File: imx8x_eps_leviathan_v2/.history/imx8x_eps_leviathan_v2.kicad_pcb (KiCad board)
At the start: 6 copper layers, 100 x 100 mm, 430 parts, among them CN1 DF11-16DP-2DSA(08), CN2 DF11-16DP-2DSA(08), J1 Conn_01x01_Socket, J10 BTH-070-02-L-D-A, J2 Conn_01x01_Socket, J3 Conn_01x01_Socket, J4 Conn_01x01_Socket, J5 DF11-16DP-2DSA, J9 BTH-070-02-L-D-A, Q1 IRLML6401, Q2 BSS138, SW1 SW_DIP_x01, SW2 KMR221GLFS, T1 WE-RJ45_7499111121A, T2 WE-RJ45_7499111121A, U1 XT60PW-F_C428722, U10 LT8612EUDE#PBF, U11 TCA4307DGKR, U12 INA260AIPWR, U13 TPS1HB08BQPWPRQ1, U14 LT8612EUDE#PBF, U15 INA260AIPWR, U16 TLV1704, U17 TLV1704, U18 BD2204GUL-E2, U19 CAT93C66VI-GT3, U2 MCP9808T-E/MS, U20 FT2232HL, U21 LP38693MP-ADJ/NOPB, U22 TXS0101DCKR, U23 TXS0101DCKR, U24 TXS0108EPWR, U25 DP83867CRRGZR, U26 MCP1824T-ADJE/OT, U27 TLV71310PDQNR, U28 74LVC2G07GW, U29 TPS22917DBVR, U3 MCP9808T-E/MS, U30 TLV62569PDDCR, U31 TXS0108EPWR, U32 TCA4307DGKR, U4 MCP9808T-E/MS, U5 TPS1HB08BQPWPRQ1, U6 LT8612EUDE#PBF, U7 INA260AIPWR, U8 TPS1HB08BQPWPRQ1, U9 LTC6902, Y1 12MHz, Y3 25MHz

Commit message: updates
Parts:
- C87: value 10nF -> 2.2nF
- moved R85 2.50 mm to (155.3, 124.0)
- moved SW1 2.50 mm to (159.2, 125.7)
- moved USB1 2.50 mm to (159.0, 131.5)
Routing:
- net Net-(U20-ADBUS1): track 0.00 -> 4.08 mm
- net Net-(U20-ACBUS5): track 0.00 -> 3.83 mm
- net Net-(U20-ACBUS4): track 0.00 -> 3.82 mm
- net Net-(U20-ADBUS2): track 0.00 -> 3.65 mm
- net Net-(U20-ACBUS3): track 0.00 -> 3.05 mm
- net Net-(U20-ADBUS3): track 0.00 -> 2.92 mm
- net Net-(U20-ACBUS6): track 0.00 -> 2.63 mm
- net Net-(U20-BDBUS0): track 0.00 -> 2.61 mm
- net Net-(U20-ADBUS4): track 0.00 -> 2.60 mm
- net Net-(U20-BDBUS3): track 0.00 -> 2.60 mm
- net Net-(U20-ACBUS2): track 0.00 -> 2.46 mm
- net Net-(U20-ACBUS7): track 0.00 -> 2.31 mm
- net Net-(U20-BDBUS1): track 0.00 -> 2.29 mm
- net Net-(U20-BDBUS2): track 0.00 -> 2.28 mm
- net Net-(U20-ADBUS5): track 0.00 -> 2.02 mm
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
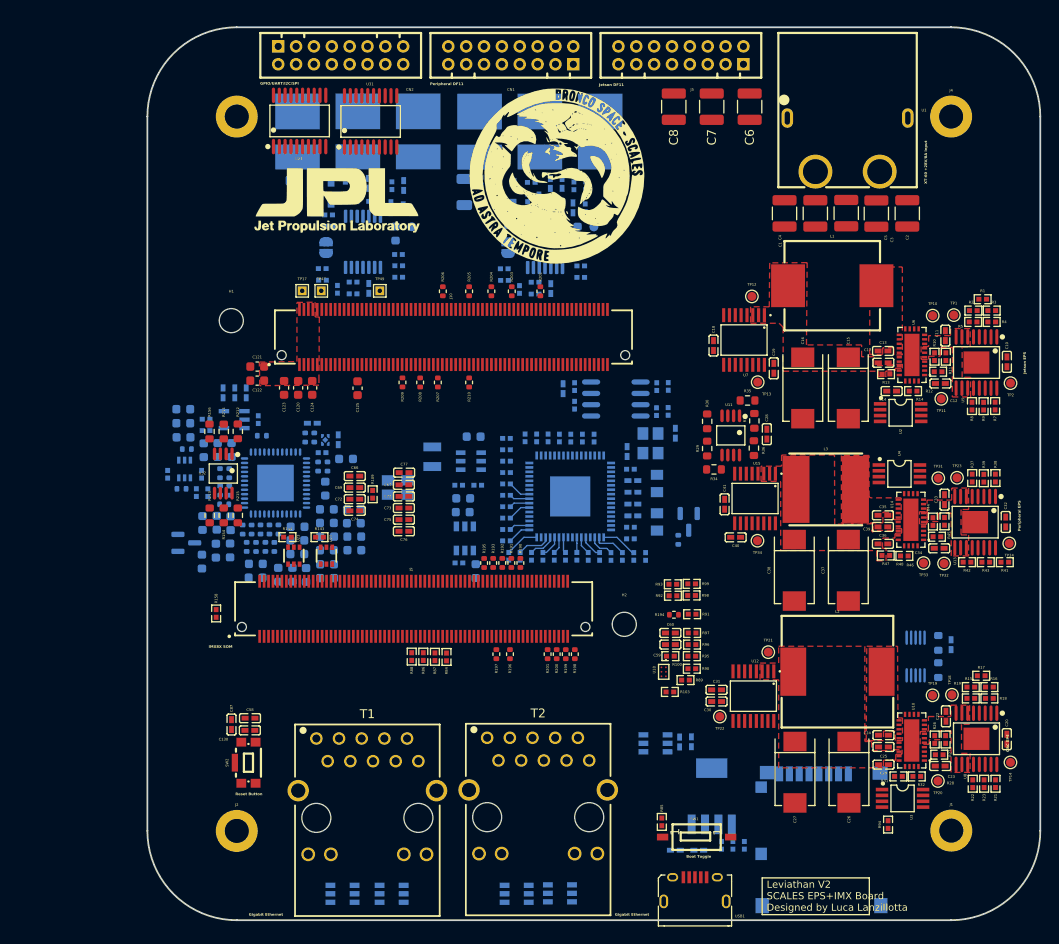
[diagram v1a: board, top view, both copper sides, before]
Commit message: Goodies
Updated USB to USB C. Added Diodes for USB. Improved Layout. Ready for some routing.
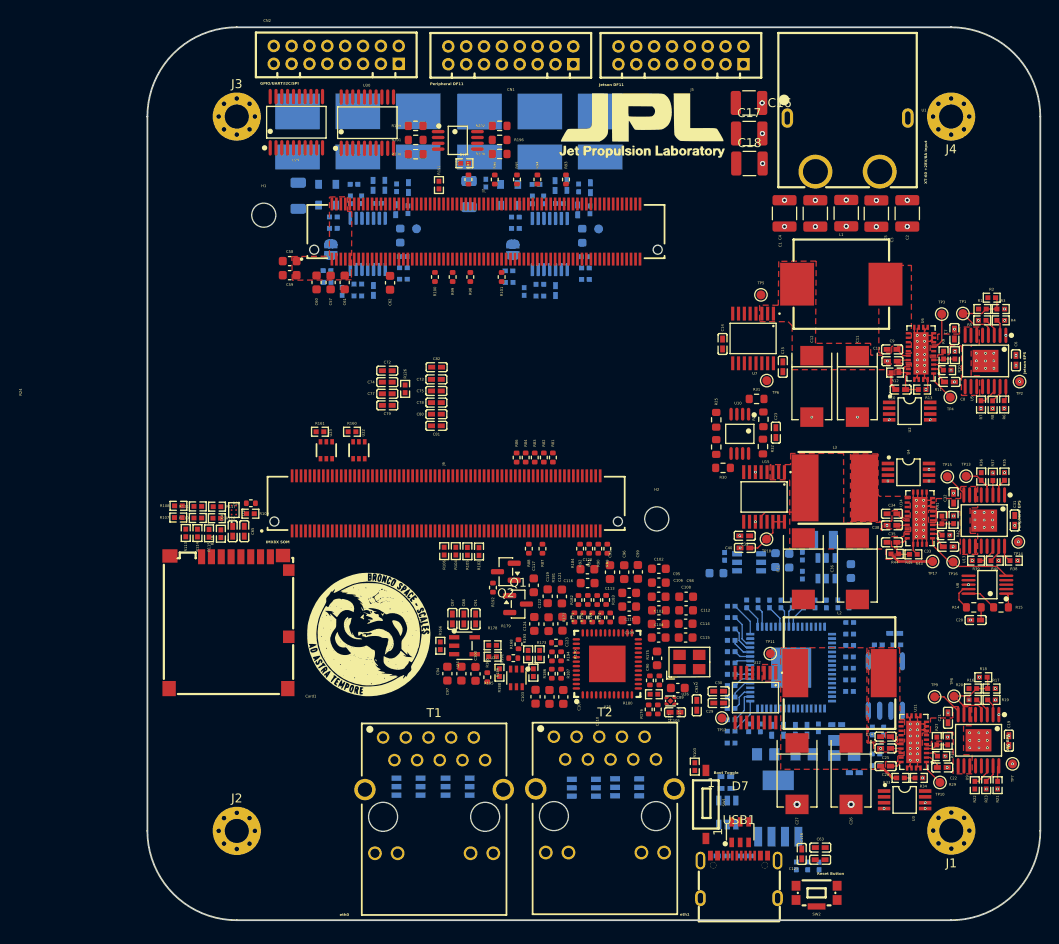
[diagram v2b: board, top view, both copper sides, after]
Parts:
- removed the C68 at (151.4, 82.5)
- removed the C7 at (160.8, 43.9)
- removed the C8 at (156.6, 43.9)
- removed the R103 at (156.2, 109.4)
- removed the TP17 at (115.0, 64.5)
- removed TP47, TP49: TestPoint, TestPoint:TestPoint_THTPad_1.0x1.0mm_Drill0.5mm
- added C17: 10u, Capacitor_SMD:C_1210_3225Metric, F.Cu at (165.0, 46.9)
- added C18: 10u, Capacitor_SMD:C_1210_3225Metric, F.Cu at (165.1, 50.2)
- added C70: 12pF, EPS:C0402, B.Cu at (174.9, 113.1)
- added D7: USBLC6-2SC6, imx8_carrier_board_footprints:SOT-23-6_L2.9-W1.6-P0.95-LS2.8-BL, F.Cu at (164.0, 125.1)
- C100: renamed from C97; moved to F.Cu
- C101: renamed from C98; moved to F.Cu
- C102: renamed from C99; moved to F.Cu
- C103: renamed from C100; moved to F.Cu
- C104: renamed from C101; moved to F.Cu
- C105: renamed from C85; moved to F.Cu
- C106: renamed from C102; moved to F.Cu
- C107: renamed from C103; moved to F.Cu
- C108: renamed from C104; moved to F.Cu
- C109: renamed from C105; moved to F.Cu
- C110: renamed from C106; moved to F.Cu
- C111: renamed from C107; moved to F.Cu
- C112: renamed from C108; moved to F.Cu
- C113: renamed from C109; moved to F.Cu
- C114: renamed from C110; moved to F.Cu
- C115: renamed from C111; moved to F.Cu
- C116: renamed from C112; moved to F.Cu
- C117: renamed from C113; moved to F.Cu
- C119: renamed from C114; moved to F.Cu
- C120: renamed from C115; moved to F.Cu
- C121: renamed from C116; moved to F.Cu
- C122: renamed from C117; moved to F.Cu
- C123: renamed from C118; moved to F.Cu
- C124: renamed from C119; moved to F.Cu
- C20: renamed from C21; moved to F.Cu
- C87: renamed from C82; moved to F.Cu
- C88: renamed from C83; moved to F.Cu
- C89: renamed from C88; moved to F.Cu
- C90: renamed from C89; moved to F.Cu
- C91: renamed from C86; moved to F.Cu
- C92: renamed from C90; moved to F.Cu
- C93: renamed from C84; moved to F.Cu
- C94: renamed from C91; moved to F.Cu
- C95: renamed from C92; moved to F.Cu
- C96: renamed from C93; moved to F.Cu
- C97: renamed from C94; moved to F.Cu
- C98: renamed from C95; moved to F.Cu
- C99: renamed from C96; moved to F.Cu
- Card1, R169, R170, R171, R172, R173, R174, R175, R176, R177, U25: moved to F.Cu
- J1, J2, J3, J4: footprint MountingHole:MountingHole_2.7mm_M2.5_DIN965_Pad -> MountingHole:MountingHole_2.7mm_M2.5_Pad_Via
- Q1, Q2: footprint imx8_carrier_board_footprints:SOT-23 -> Package_TO_SOT_SMD:SOT-23; moved to F.Cu
- R14: renamed from R24; moved to F.Cu
- R15: renamed from R25; moved to F.Cu
- R165: renamed from R167; moved to F.Cu
- R166: renamed from R148; moved to F.Cu
- R167: renamed from R168; moved to F.Cu
- R168: renamed from R189; moved to F.Cu
- R178: renamed from R155; moved to F.Cu
- R179: renamed from R157; moved to F.Cu
- R180: renamed from R151; moved to F.Cu
- R181: renamed from R179; moved to F.Cu
- R182: renamed from R180; moved to F.Cu
- R183: renamed from R181; moved to F.Cu
- R184: renamed from R182; moved to F.Cu
- R186: renamed from R183; moved to F.Cu
- R187: renamed from R184; moved to F.Cu
- R188: renamed from R149; moved to F.Cu
- R189: renamed from R150; moved to F.Cu
- R190: renamed from R152; moved to F.Cu
- R191: renamed from R153; moved to F.Cu
- R192: renamed from R185; moved to F.Cu
- R193: renamed from R186; moved to F.Cu
- R194: renamed from R187; moved to F.Cu
- R195: renamed from R188; moved to F.Cu
- U24: renamed from U26; moved to F.Cu
- U26: renamed from U27; moved to F.Cu
- U27: renamed from U28; moved to F.Cu
- U8: renamed from U9; moved to F.Cu
- USB1: value 10118194-0001LF -> TYPE-C 16PIN 2MD; footprint imx8_carrier_board_footprints:MICRO-USB-SMD_10118194-0001LF -> imx8_carrier_board_footprints:USB-C-SMD_TYPE-C-6PIN-2MD-073
- Y2: renamed from Y3; moved to F.Cu
- moved R112 88.0 mm to (133.2, 50.2), turned to 0 degrees
- moved Card1 70.6 mm to (106.8, 101.6), turned to 180 degrees
- moved SW2 65.7 mm to (172.6, 132.3), turned to 180 degrees
- moved C118 65.5 mm to (170.9, 127.5)
- moved C125 65.5 mm to (173.0, 128.2)
- moved C63 65.5 mm to (173.0, 126.8)
- moved R108 60.3 mm to (101.1, 88.6), turned to 180 degrees
- moved R107 59.6 mm to (101.1, 89.9), turned to 180 degrees
- moved R113 58.3 mm to (101.9, 91.6), turned to 90 degrees
- moved R114 56.8 mm to (103.3, 91.6), turned to 90 degrees
- moved G*** 55.5 mm to (122.5, 102.9)
- moved R115 55.2 mm to (104.6, 91.6), turned to 90 degrees
- moved R197 54.1 mm to (130.3, 52.6)
- moved R110 53.9 mm to (103.3, 89.9)
- moved R111 53.9 mm to (103.3, 88.6)
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- renumbered C14 to C10, C15 to C11, C87 to C118, C16 to C12, C130 to C125, C17 to C13, C126 to C130, C127 to C131, C128 to C132, C129 to C133, C18 to C14, C19 to C15, C6 to C16, C20 to C19, C22 to C21, C23 to C22, C28 to C23, C29 to C28, C30 to C29, C31 to C30, C32 to C31, C33 to C32, C34 to C33, C35 to C34, C36 to C35, C37 to C36, C38 to C37, C39 to C38, C40 to C39, C41 to C40, C42 to C41, C43 to C42, C44 to C43, C45 to C44, C46 to C45, C47 to C46, C48 to C47, C49 to C48, C50 to C49, C51 to C50, C52 to C51, C53 to C52, C54 to C53, C55 to C54, C56 to C55, C57 to C56, C120 to C57, C121 to C58, C122 to C59, C10 to C6, C123 to C60, C124 to C61, C125 to C62, C58 to C63, C59 to C64, C60 to C65, C61 to C66, C62 to C67, C63 to C68, C64 to C69, C11 to C7, C65 to C71, C66 to C72, C67 to C73, C69 to C74, C70 to C75, C71 to C76, C72 to C77, C73 to C78, C74 to C79, C12 to C8, C75 to C80, C76 to C81, C77 to C82, C78 to C83, C79 to C84, C80 to C85, C81 to C86, C13 to C9, D4 to D1, D5 to D2, D6 to D3, D7 to D4, D8 to D5, D9 to D6, J9 to J6, J10 to J7, R2 to R1, R11 to R10, R209 to R100, R210 to R101, R84 to R102, R85 to R103, R86 to R104, R87 to R105, R88 to R106, R89 to R107, R90 to R108, R91 to R109, R12 to R11, R92 to R110, R93 to R111, R94 to R112, R95 to R113, R96 to R114, R97 to R115, R98 to R116, R99 to R117, R100 to R118, R13 to R12, R102 to R120, R104 to R121, R105 to R122, R106 to R123, R107 to R124, R108 to R125, R109 to R126, R110 to R127, R111 to R128, R112 to R129, R14 to R13, R113 to R130, R114 to R131, R115 to R132, R116 to R133, R117 to R134, R118 to R135, R119 to R136, R120 to R137, R121 to R138, R122 to R139, R123 to R140, R124 to R141, R125 to R142, R126 to R143, R127 to R144, R128 to R145, R129 to R146, R130 to R147, R131 to R148, R132 to R149, R133 to R150, R134 to R151, R135 to R152, R136 to R153, R137 to R154, R138 to R155, R139 to R156, R140 to R157, R141 to R158, R142 to R159, R15 to R16, R143 to R160, R144 to R161, R145 to R162, R146 to R163, R147 to R164, R16 to R17, R17 to R18, R18 to R19, R154 to R196, R158 to R197, R156 to R198, R212 to R199, R1 to R2, R19 to R20, R213 to R200, R214 to R201, R215 to R202, R6 to R212, R20 to R213, R29 to R24, R30 to R25, R33 to R26, R26 to R27, R27 to R28, R28 to R29, R34 to R30, R35 to R31, R36 to R32, R31 to R33, R32 to R34, R38 to R35, R37 to R36, R39 to R37, R41 to R38, R42 to R39, R43 to R40, R44 to R41, R45 to R42, R46 to R43, R47 to R44, R48 to R45, R49 to R46, R50 to R47, R51 to R48, R52 to R49, R53 to R50, R54 to R51, R55 to R52, R56 to R53, R57 to R54, R58 to R55, R59 to R56, R60 to R57, R61 to R58, R62 to R59, R7 to R6, R63 to R60, R64 to R61, R65 to R62, R66 to R63, R67 to R64, R68 to R65, R69 to R66, R70 to R67, R71 to R68, R72 to R69, R8 to R7, R73 to R70, R74 to R71, R75 to R72, R76 to R73, R77 to R74, R78 to R75, R79 to R76, R80 to R77, R81 to R78, R82 to R79, R9 to R8, R83 to R80, R190 to R81, R191 to R82, R192 to R83, R193 to R84, R194 to R85, R195 to R86, R196 to R87, R197 to R88, R198 to R89, R10 to R9, R199 to R90, R200 to R91, R201 to R92, R202 to R93, R203 to R94, R204 to R95, R205 to R96, R206 to R97, R207 to R98, R208 to R99, TP20 to TP10, TP21 to TP11, TP22 to TP12, TP23 to TP13, TP24 to TP14, TP31 to TP15, TP32 to TP16, TP33 to TP17, TP34 to TP18, TP36 to TP19, TP42 to TP20, TP10 to TP3, TP11 to TP4, TP12 to TP5, TP13 to TP6, TP14 to TP7, TP18 to TP8, TP19 to TP9, U11 to U10, U10 to U11, U32 to U28, U24 to U29, U31 to U30, U29 to U31, U30 to U32, U8 to U9
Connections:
- C71 pad 1: GND -> /IMX8XQXP SCALES Mariner Carrier Board/Debug USB - UART/FTDI_OSCO
- C71 pad 2: /IMX8XQXP SCALES Mariner Carrier Board/Debug USB - UART/FTDI_OSCO -> GND
- CN2 pad 1: Net-(U24-B1) -> GND
- CN2 pad 10: Net-(U31-B5) -> Net-(U30-B4)
- CN2 pad 11: Net-(U24-B6) -> Net-(U29-B3)
- CN2 pad 12: Net-(U31-B6) -> Net-(U30-B3)
- CN2 pad 13: Net-(U24-B7) -> Net-(U29-B2)
- CN2 pad 14: Net-(U31-B7) -> I2C3_USR_SCL
- CN2 pad 15: GND -> Net-(U29-B1)
- CN2 pad 16: GND -> I2C3_USR_SDA
- CN2 pad 2: I2C3_USR_SDA -> GND
- CN2 pad 3: Net-(U24-B2) -> Net-(U29-B7)
- CN2 pad 4: I2C3_USR_SCL -> Net-(U30-B7)
- CN2 pad 5: Net-(U24-B3) -> Net-(U29-B6)
- CN2 pad 6: Net-(U31-B3) -> Net-(U30-B6)
- CN2 pad 7: Net-(U24-B4) -> Net-(U29-B5)
- CN2 pad 8: Net-(U31-B4) -> Net-(U30-B5)
- CN2 pad 9: Net-(U24-B5) -> Net-(U29-B4)
- JP1 pad 1: Net-(JP1-A) -> unconnected-(JP1-A-Pad1)
- JP1 pad 2: ~{WD_EN_OBC} -> unconnected-(JP1-B-Pad2)
- JP2 pad 1: Net-(JP2-A) -> unconnected-(JP2-A-Pad1)
- JP2 pad 2: ~{WD_EN_JETSON} -> unconnected-(JP2-B-Pad2)
- U16 pad 13: Net-(JP1-A) -> unconnected-(U16-Pad13)
- U17 pad 13: Net-(JP2-A) -> unconnected-(U17-Pad13)
- U29 pad 13: Net-(U24-B7) -> Net-(U29-B7)
- U29 pad 14: Net-(U24-B6) -> Net-(U29-B6)
- U29 pad 15: Net-(U24-B5) -> Net-(U29-B5)
- U29 pad 16: Net-(U24-B4) -> Net-(U29-B4)
- U29 pad 17: Net-(U24-B3) -> Net-(U29-B3)
- U29 pad 18: Net-(U24-B2) -> Net-(U29-B2)
- U29 pad 20: Net-(U24-B1) -> Net-(U29-B1)
- U30 pad 13: Net-(U31-B7) -> Net-(U30-B7)
- U30 pad 14: Net-(U31-B6) -> Net-(U30-B6)
- U30 pad 15: Net-(U31-B5) -> Net-(U30-B5)
- U30 pad 16: Net-(U31-B4) -> Net-(U30-B4)
- U30 pad 17: Net-(U31-B3) -> Net-(U30-B3)
- USB1 pad 1: VBUS_DEBUG_USB -> GND
- USB1 pad 2: /IMX8XQXP SCALES Mariner Carrier Board/Debug USB - UART/DEBUG_USB_DN -> VBUS_DEBUG_USB
- USB1 pad 3: /IMX8XQXP SCALES Mariner Carrier Board/Debug USB - UART/DEBUG_USB_DP -> unconnected-(USB1-SBU2-Pad3)
- USB1 pad 4: /IMX8XQXP SCALES Mariner Carrier Board/Debug USB - UART/DEBUG_USB_ID -> Net-(USB1-CC1)
- USB1 pad 5: GND -> Net-(USB1-DN1)
- USB1 pad 6: GND -> Net-(USB1-DP1)
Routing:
- net GND: track 0.00 -> 32.2 mm, vias 0 -> 105
- net SYNC_PHASE2: track 0.00 -> 10.4 mm
- net Net-(U9-EN): track 0.00 -> 9.74 mm
- net Net-(U5-EN): track 0.00 -> 9.73 mm
- net Net-(U14-BIAS): track 0.00 -> 9.58 mm
- net +5V_Perif: track 0.00 -> 5.82 mm
- net Net-(U6-FB): track 0.00 -> 4.44 mm
- net Net-(U5-VOUT): track 0.00 -> 4.19 mm
- net Net-(U14-FB): track 0.00 -> 3.97 mm
- net Net-(U13-EN): track 0.00 -> 3.80 mm
- net Net-(U11-VIN): track 0.00 -> 3.70 mm
- net Net-(U8-SET): track 0.00 -> 3.45 mm
- net SYNC_PHASE3: track 0.00 -> 3.43 mm
- net Net-(U8-MOD): track 0.00 -> 3.19 mm
- net +3.3V_OBC: track 0.00 -> 3.09 mm
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- added copper zone on In2.Cu, net +V_Batt
- added copper zone on In1.Cu, net GND
- added copper zone on In4.Cu, net GND
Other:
- board text added: "eth0"
- board text added: "eth1"
- board text removed: "Gigabit Ethernet"
- board text removed: "Leviathan V2 SCALES EPS+IMX Board Designed by Luca Lanzillotta"

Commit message: Started routing
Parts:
- D7: moved to B.Cu
- moved R122 6.32 mm to (177.2, 111.7), turned to -90 degrees
- moved R120 6.06 mm to (175.9, 111.3), turned to -90 degrees
- moved D7 5.74 mm to (163.8, 130.8)
- moved R123 5.08 mm to (183.4, 111.6)
- moved R121 0.95 mm to (179.3, 113.3), turned to 0 degrees
- moved R129 0.43 mm to (165.0, 113.8)
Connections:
- CN2 pad 1: GND -> Net-(U29-B1)
- CN2 pad 10: Net-(U30-B4) -> Net-(U30-B5)
- CN2 pad 11: Net-(U29-B3) -> Net-(U29-B6)
- CN2 pad 12: Net-(U30-B3) -> Net-(U30-B6)
- CN2 pad 13: Net-(U29-B2) -> Net-(U29-B7)
- CN2 pad 14: I2C3_USR_SCL -> Net-(U30-B7)
- CN2 pad 15: Net-(U29-B1) -> GND
- CN2 pad 16: I2C3_USR_SDA -> GND
- CN2 pad 2: GND -> I2C3_USR_SDA
- CN2 pad 3: Net-(U29-B7) -> Net-(U29-B2)
- CN2 pad 4: Net-(U30-B7) -> I2C3_USR_SCL
- CN2 pad 5: Net-(U29-B6) -> Net-(U29-B3)
- CN2 pad 6: Net-(U30-B6) -> Net-(U30-B3)
- CN2 pad 7: Net-(U29-B5) -> Net-(U29-B4)
- CN2 pad 8: Net-(U30-B5) -> Net-(U30-B4)
- CN2 pad 9: Net-(U29-B4) -> Net-(U29-B5)
- USB1 pad 5: Net-(USB1-DN1) -> /IMX8XQXP SCALES Mariner Carrier Board/Debug USB - UART/DEBUG_USB_DN
- USB1 pad 6: Net-(USB1-DP1) -> /IMX8XQXP SCALES Mariner Carrier Board/Debug USB - UART/DEBUG_USB_DP
- USB1 pad 7: Net-(USB1-DN1) -> /IMX8XQXP SCALES Mariner Carrier Board/Debug USB - UART/DEBUG_USB_DN
- USB1 pad 8: Net-(USB1-DP1) -> /IMX8XQXP SCALES Mariner Carrier Board/Debug USB - UART/DEBUG_USB_DP
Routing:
- net GND: track 32.2 -> 70.4 mm, vias 105 -> 158
- net ETH1_B_TX_N: track 0.00 -> 21.0 mm
- net 3V3_FTDI: track 0.00 -> 17.5 mm
- net ETH1_C_TXCLK_P: track 0.00 -> 14.7 mm
- net ETH1_A_TX_N: track 0.00 -> 13.5 mm
- net ETH1_D_RXDV_P: track 0.00 -> 12.8 mm
- net ETH1_C_TXCLK_N: track 0.00 -> 12.5 mm
- net ETH1_B_TX_P: track 0.00 -> 11.8 mm
- net ETH1_A_TX_P: track 0.00 -> 11.8 mm
- net Net-(U19-CS): track 0.00 -> 11.1 mm
- net Net-(U19-SK): track 0.00 -> 10.4 mm
- net Net-(U20-EEDATA): track 0.00 -> 10.1 mm
- net ETH1_D_RXDV_N: track 0.00 -> 9.97 mm
- net VBUS_DEBUG_USB: track 0.00 -> 8.37 mm, vias 0 -> 1
- net Net-(U20-VPHY): track 0.00 -> 7.71 mm
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
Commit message: More routing
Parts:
- removed D7: USBLC6-2SC6, imx8_carrier_board_footprints:SOT-23-6_L2.9-W1.6-P0.95-LS2.8-BL
- removed Y1: 12MHz, imx8_carrier_board_footprints:CRYSTAL-SMD_4P-L3.2-W2.5-BL
- J1, J2, J3, J4: footprint MountingHole:MountingHole_2.7mm_M2.5_Pad_Via -> MountingHole:MountingHole_3.2mm_M3_Pad_Via
- R110, R111, R116, R117: moved to B.Cu
- moved R199 33.6 mm to (111.5, 75.4), turned to 90 degrees
- moved R202 32.5 mm to (111.5, 66.0), turned to -90 degrees
- moved R201 31.5 mm to (113.1, 75.4), turned to 90 degrees
- moved R196 30.3 mm to (113.1, 66.0), turned to -90 degrees
- moved U28 30.1 mm to (113.1, 70.7), turned to 0 degrees
- moved R198 29.3 mm to (114.7, 75.4), turned to 90 degrees
- moved R200 28.1 mm to (114.7, 66.0), turned to -90 degrees
- moved R112 26.4 mm to (115.7, 70.0), turned to 90 degrees
- moved R111 12.8 mm to (110.3, 99.3), turned to -90 degrees
- moved R110 11.0 mm to (109.0, 99.3), turned to -90 degrees
- moved R117 9.80 mm to (110.3, 97.2), turned to -90 degrees
- moved R116 8.08 mm to (109.0, 97.2), turned to -90 degrees
- moved R85 3.28 mm to (109.5, 91.5), turned to 0 degrees
- moved R109 3.28 mm to (109.4, 92.7)
- moved U18 3.25 mm to (104.3, 90.2), turned to 0 degrees
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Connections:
- CN2 pad 1: Net-(U29-B1) -> I2C3_USR_SDA
- CN2 pad 10: Net-(U30-B5) -> Net-(U29-B5)
- CN2 pad 11: Net-(U29-B6) -> Net-(U30-B6)
- CN2 pad 12: Net-(U30-B6) -> Net-(U29-B6)
- CN2 pad 13: Net-(U29-B7) -> Net-(U30-B7)
- CN2 pad 14: Net-(U30-B7) -> Net-(U29-B7)
- CN2 pad 2: I2C3_USR_SDA -> Net-(U29-B1)
- CN2 pad 3: Net-(U29-B2) -> I2C3_USR_SCL
- CN2 pad 4: I2C3_USR_SCL -> Net-(U29-B2)
- CN2 pad 5: Net-(U29-B3) -> Net-(U30-B3)
- CN2 pad 6: Net-(U30-B3) -> Net-(U29-B3)
- CN2 pad 7: Net-(U29-B4) -> Net-(U30-B4)
- CN2 pad 8: Net-(U30-B4) -> Net-(U29-B4)
- CN2 pad 9: Net-(U29-B5) -> Net-(U30-B5)
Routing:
- net VCC_LDO_SD1: track 0.00 -> 20.4 mm, vias 0 -> 3
- net /SCALES_EPS/OBC_Subsystem/WD_OBC/WDT-VIN: track 0.00 -> 16.6 mm
- net +1.8V_OBC_Perif: track 3.47 -> 20.0 mm
- net Net-(U17E-V+): track 0.00 -> 15.4 mm
- net VDD_ETH_1V0: track 0.00 -> 14.6 mm
- net ETH1_D_RXDV_P: track 12.8 -> 19.4 mm
- net ETH1_B_TX_P: track 11.8 -> 18.0 mm
- net ETH1_A_TX_P: track 11.8 -> 17.6 mm
- net Net-(U16C--): track 0.00 -> 5.68 mm
- net X_CONN_USDHC1_CLK: track 0.00 -> 5.67 mm
- net Net-(Card1-VDD): track 0.00 -> 5.30 mm
- net ETH1_C_TXCLK_N: track 12.5 -> 17.4 mm
- net ETH1_D_RXDV_N: track 9.97 -> 14.4 mm
- net Net-(C44-Pad2): track 0.00 -> 3.99 mm
- net X_BOOT_MODE0: track 0.00 -> 3.61 mm
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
